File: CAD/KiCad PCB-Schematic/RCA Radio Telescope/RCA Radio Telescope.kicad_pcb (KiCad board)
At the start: 2 copper layers, 60 x 40 mm, 34 parts, among them J2 5V From PoE Splitter, J3 3V Out For LNA, J4 5V Out For Filter Board, J7 USB_A, J8 USB_A, Q1 DMP4047LFDE-7, U13 MAX8510EXK30T, U14 TPS62133RGTR

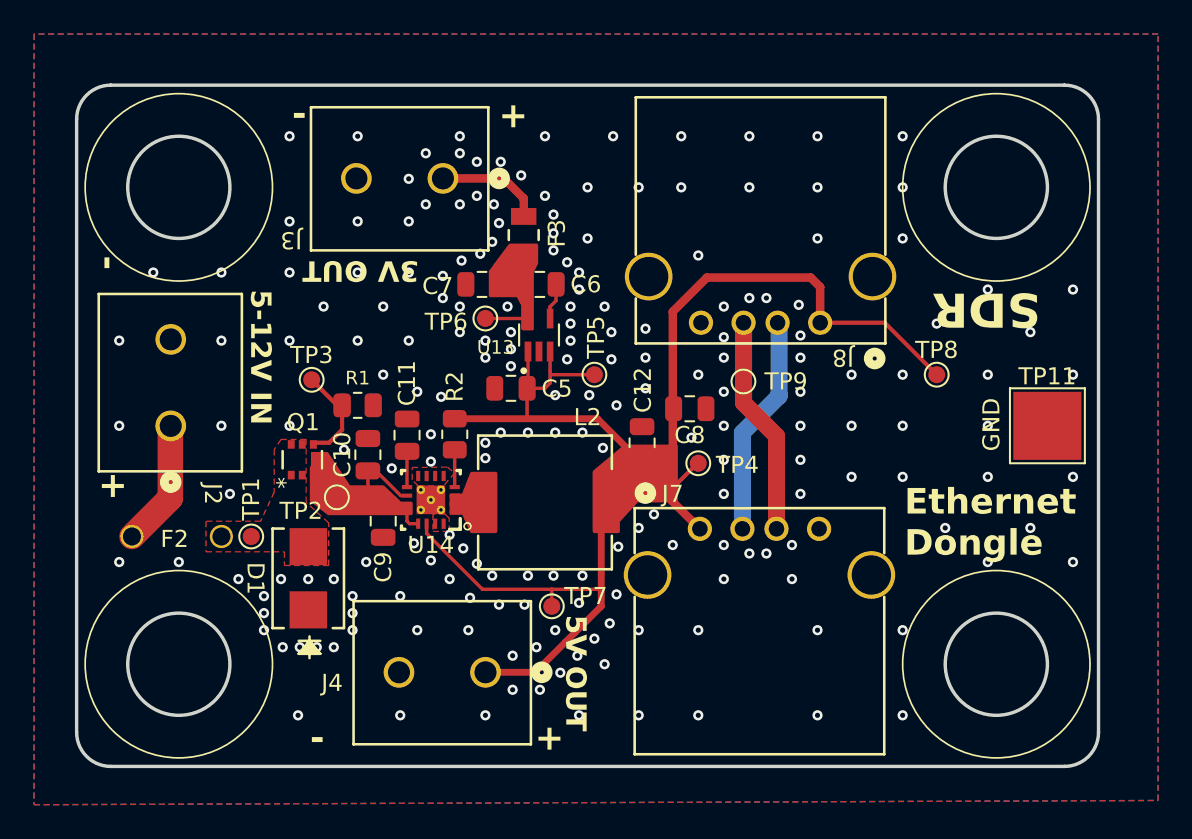
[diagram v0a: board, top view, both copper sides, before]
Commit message: Updated PowerData Schematic to v2.0 and PCB to v1.9
- Added 0 Ohm resistors to modularized PCB
- Adjusted some GND vias to prevent clipping of silkscreen
- Edited LDO footprint to adhere with JLC specs
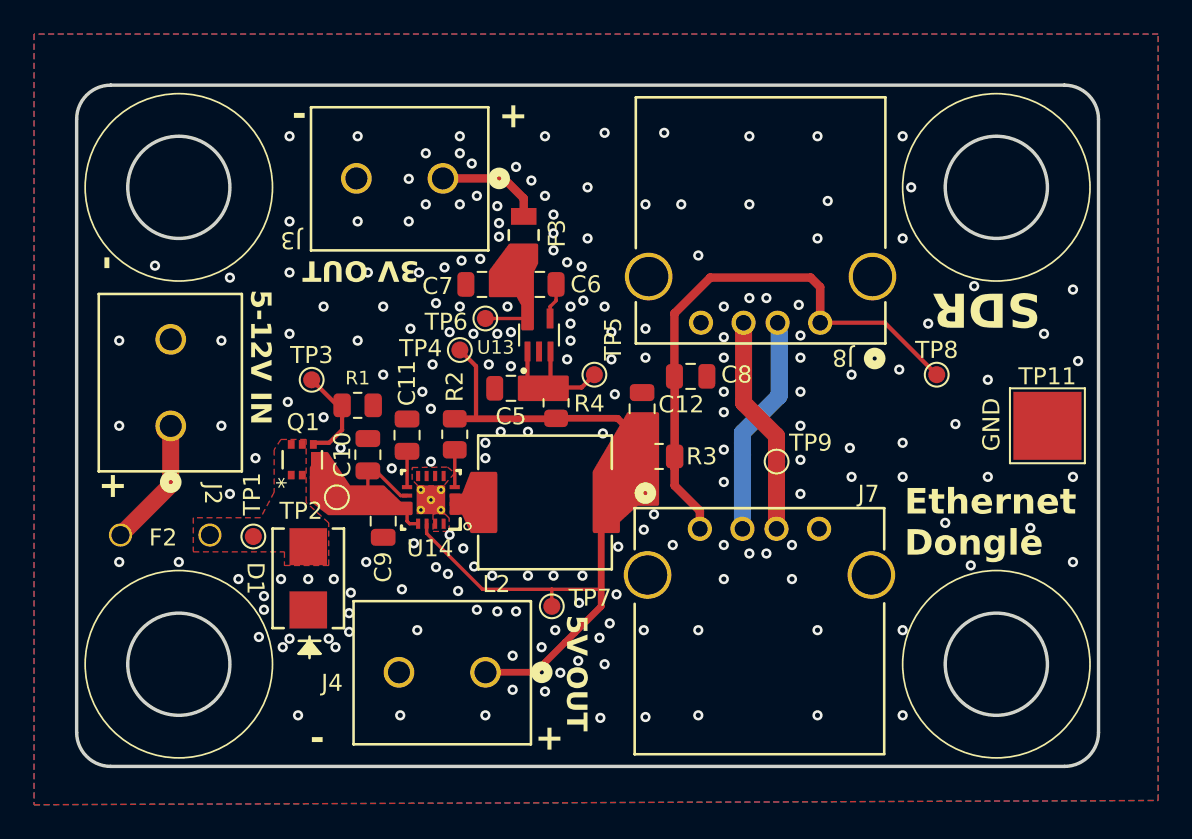
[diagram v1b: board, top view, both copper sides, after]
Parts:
- added R3: 0, Resistor_SMD:R_0805_2012Metric, F.Cu at (48.2, 35.8)
- added R4: 0, Resistor_SMD:R_0805_2012Metric, F.Cu at (42.1, 32.6)
- moved TP4 15.5 mm to (36.5, 29.6), turned to 90 degrees
- moved TP9 5.09 mm to (55.1, 36.1)
- moved C12 2.00 mm to (47.2, 33.0)
- moved C8 1.90 mm to (50.0, 31.1)
- moved F2 0.68 mm to (19.6, 44.4)
- moved TP1 0.12 mm to (24.4, 40.5)
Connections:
- C5 pad 1: +5V -> Net-(U13-IN)
- C8 pad 1: +5V -> /PowerDataDistribute/USB_5V_IN
- J7 pad 1: +5V -> /PowerDataDistribute/USB_5V_IN
- J8 pad 1: +5V -> /PowerDataDistribute/USB_5V_IN
- TP5 pad 1: +5V -> Net-(U13-IN)
- TP8 pad 1: +5V -> /PowerDataDistribute/USB_5V_IN
- U13 pad 1: +5V -> Net-(U13-IN)
- U13 pad 3: +5V -> Net-(U13-IN)
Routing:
- net +5V: track 85.5 -> 40.7 mm
- net /PowerDataDistribute/USB_5V_IN: track 0.00 -> 33.1 mm
- net Net-(U13-IN): track 0.00 -> 5.52 mm
- net GND: vias 200 -> 195
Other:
- board text added: "PSU ECE Capstone Team 11 - RCA Telescope v1.9 (3/28/2025)"
- board text removed: "PSU ECE Capstone Team 11 - RCA Telescope v1.8 (3/27/2025)"

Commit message: Updated PowerData PCB to v2.0
- Readjusted some via holes and grounding for Buck
- Adjusted location for testpoint and silkscreens
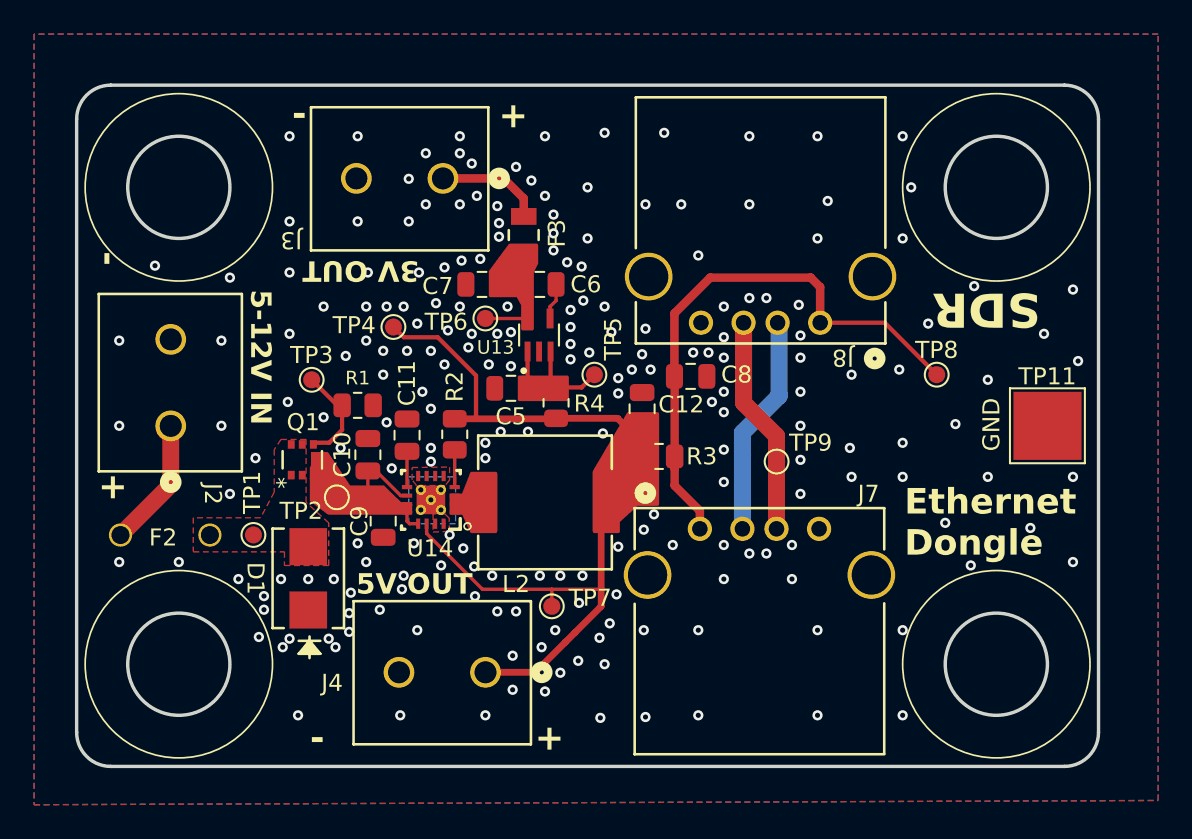
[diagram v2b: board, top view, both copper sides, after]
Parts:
- moved TP4 4.13 mm to (32.6, 28.2)
- moved TP1 0.09 mm to (24.4, 40.4)
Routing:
- net +5V: track 40.7 -> 44.9 mm
- net GND: vias 195 -> 211
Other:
- board text added: "PSU ECE Capstone Team 11 - RCA Telescope v2.0 (3/28/2025)"
- board text removed: "PSU ECE Capstone Team 11 - RCA Telescope v1.9 (3/28/2025)"

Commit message: Updated PowerData PCB to v2.1
- Added custom JLC rules from https://github.com/Cimos/KiCad-CustomDesignRules/tree/main
- Adjusted silkscreen according to new rules
- Added step models for components
- Adjusted via locations to be more spread out
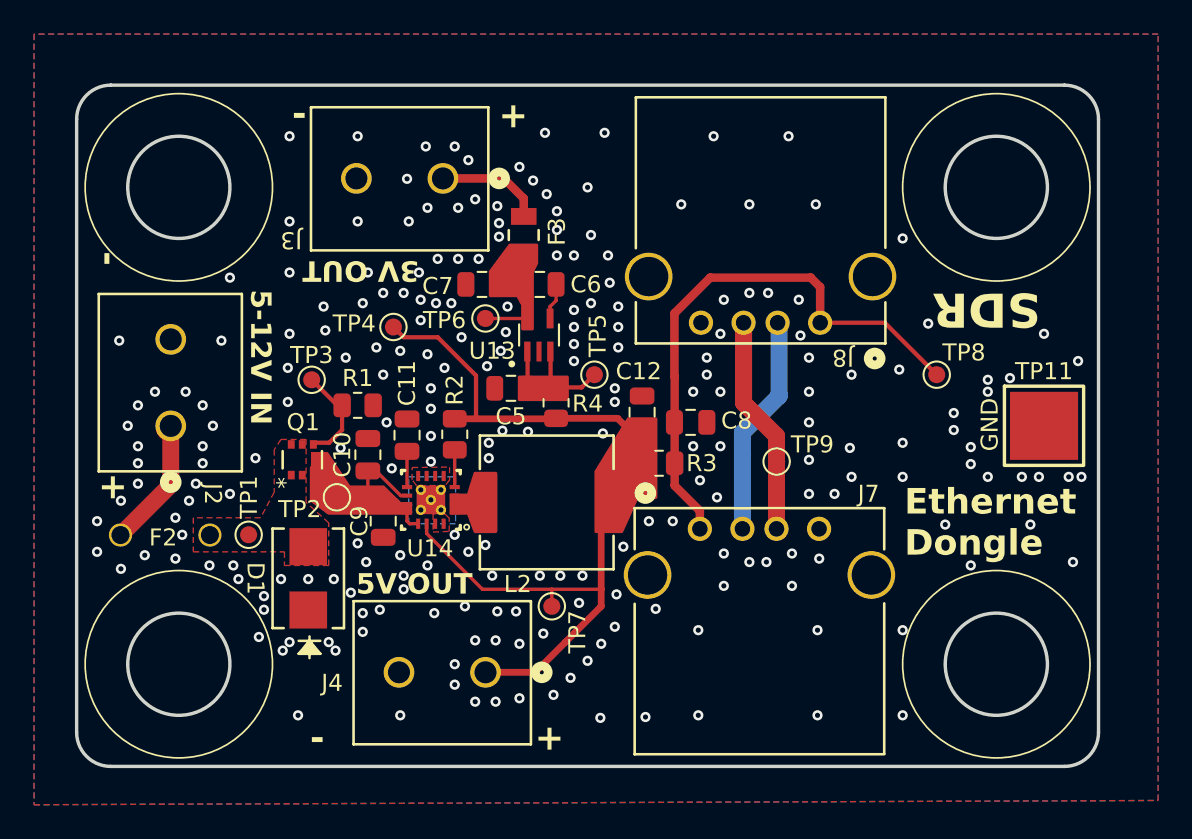
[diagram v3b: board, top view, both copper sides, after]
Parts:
- TP1, TP10, TP2, TP3, TP4, TP5, TP6, TP7, TP8, TP9: footprint TestPoint:TestPoint_Pad_D1.0mm -> Library:TestPoint_Pad_D1.0mm_Edit
- TP11: footprint TestPoint:TestPoint_Pad_4.0x4.0mm -> Library:TestPoint_Pad_4.0x4.0mm_Edit
- moved G*** 10.3 mm to (28.4, 32.6)
- moved C8 2.70 mm to (50.0, 33.8)
- moved R3 0.40 mm to (48.2, 36.2)
- moved TP1 0.28 mm to (24.1, 40.4)
- moved C12 0.20 mm to (47.2, 33.2)
- moved TP11 0.20 mm to (70.8, 34.0)
- moved L2 0.10 mm to (41.6, 38.5)
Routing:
- net GND: vias 211 -> 227
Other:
- board text added: "PSU ECE Capstone Team 11 RCA Radio Telescope v2.1 (3/29/2025)"
- board text removed: "PSU ECE Capstone Team 11 - RCA Telescope v2.0 (3/28/2025)"

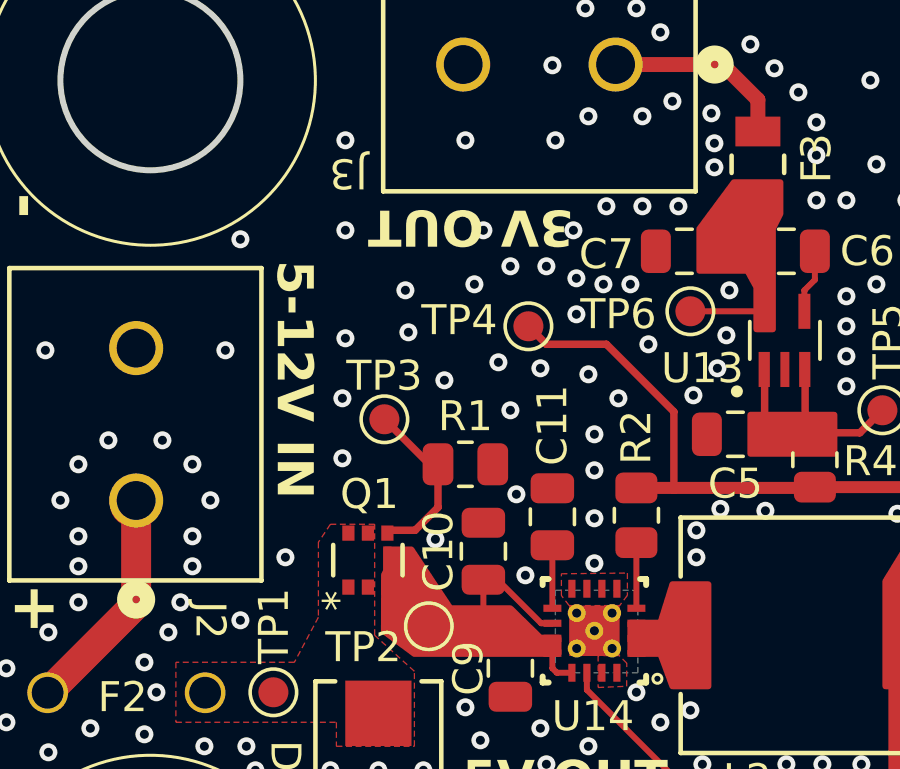
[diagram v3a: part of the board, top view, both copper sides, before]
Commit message: Updated Root Schematic to v1.6 and P/D PCB to v2.2
- Changed input voltage to P/D board to 9-12V (Concerned about voltage drop of components which may not allow for 5V out)
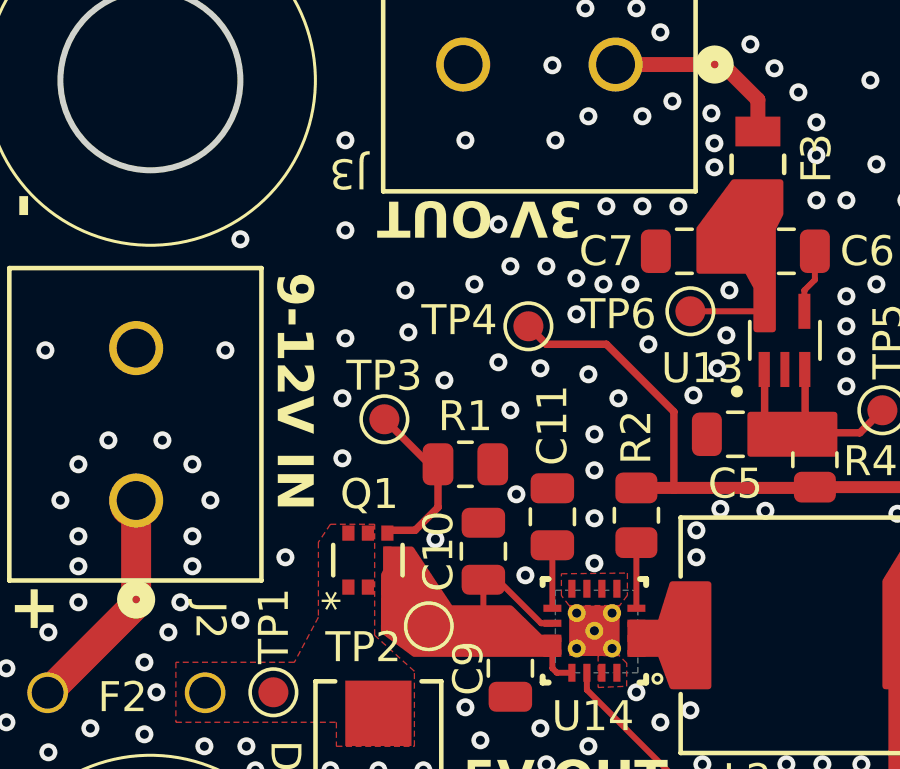
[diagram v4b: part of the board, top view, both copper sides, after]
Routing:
- net GND: vias 227 -> 226
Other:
- board text added: "9-12V IN"
- board text added: "PSU ECE Capstone Team 11 RCA Radio Telescope v2.2 (3/29/2025)"
- board text removed: "5-12V IN"
- board text removed: "PSU ECE Capstone Team 11 RCA Radio Telescope v2.1 (3/29/2025)"
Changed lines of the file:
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@@
 		(title "Power Data Distribute PCB")
 		(date "2025-03-29")
-		(rev "2.1")
+		(rev "2.2")
 	)
 	(layers
@@
 		(tags "capacitor")
 		(property "Reference" "C7"
-			(at 2.6 -0.1 180)
+			(at 2.6 0 0)
 			(layer "F.SilkS")
 			(effects
@@
 		(layer "Edge.Cuts")
 	)
-	(gr_text "PSU ECE Capstone\nTeam 11\nRCA Radio Telescope\nv2.1 (3/29/2025)"
+	(gr_text "PSU ECE Capstone\nTeam 11\nRCA Radio Telescope\nv2.2 (3/29/2025)"
 		(at 62 23 0)
 		(layer "B.SilkS")
@@
 		)
 	)
-	(gr_text "5-12V IN"
-		(at 24.1 26 270)
+	(gr_text "9-12V IN"
+		(at 24.1 26.4 270)
 		(layer "F.SilkS")
 		(effects
@@
 	)
 	(gr_text "3V OUT"
-		(at 34.1 24.2 180)
+		(at 34.4 23.9 180)
 		(layer "F.SilkS")
 		(effects
@@
 	)
 	(via
-		(at 31.1 25)
+		(at 31.6 24.8)
 		(size 0.6)
 		(drill 0.3)
@@
 		(size 0.6)
 		(drill 0.3)
-		(layers "F.Cu" "B.Cu")
-		(free yes)
-		(net 1)
-	)
-	(via
-		(at 34.1 25)
-		(size 0.6)
-		(drill 0.3)
